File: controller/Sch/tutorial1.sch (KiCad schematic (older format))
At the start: 4 parts

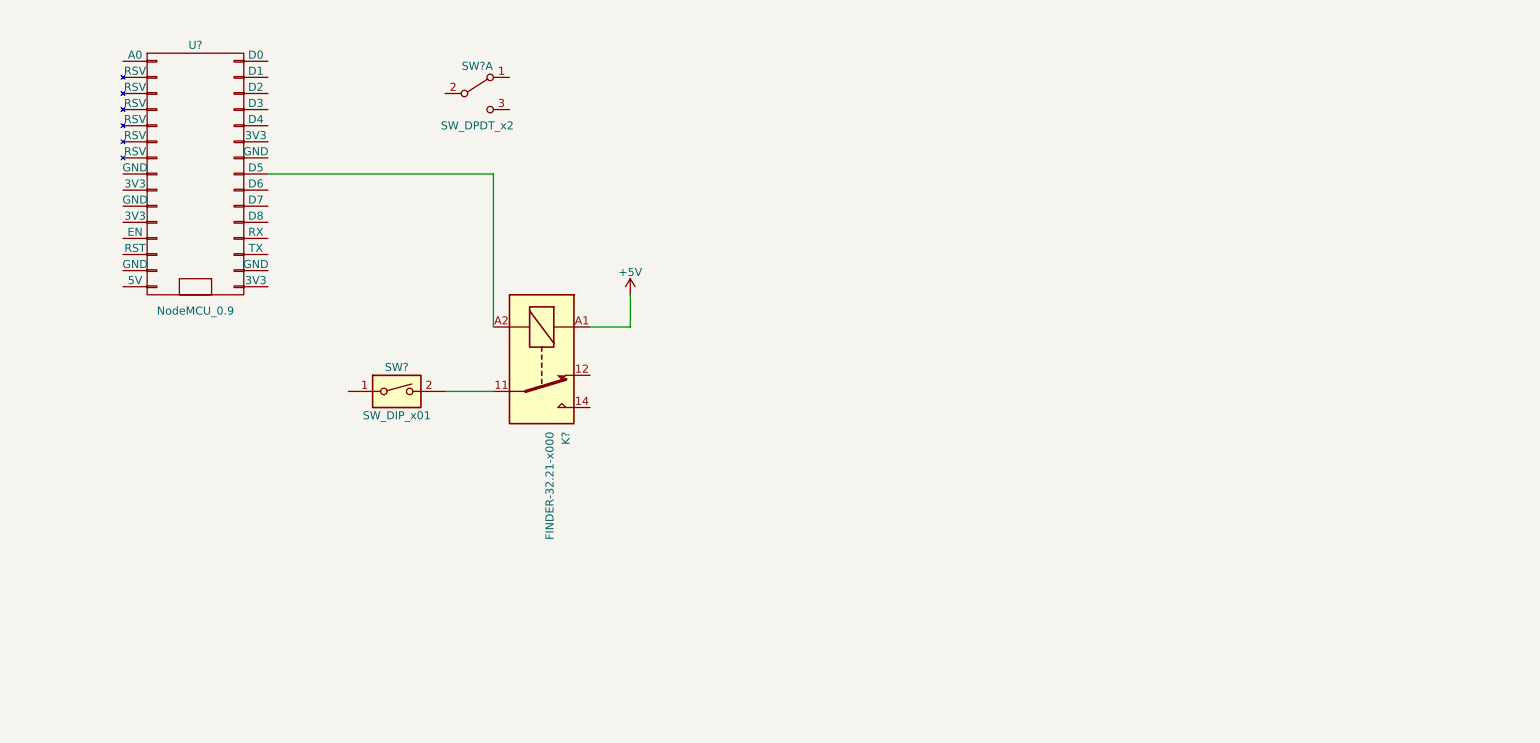
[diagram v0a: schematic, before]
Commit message: Added couple of the switches circuits.
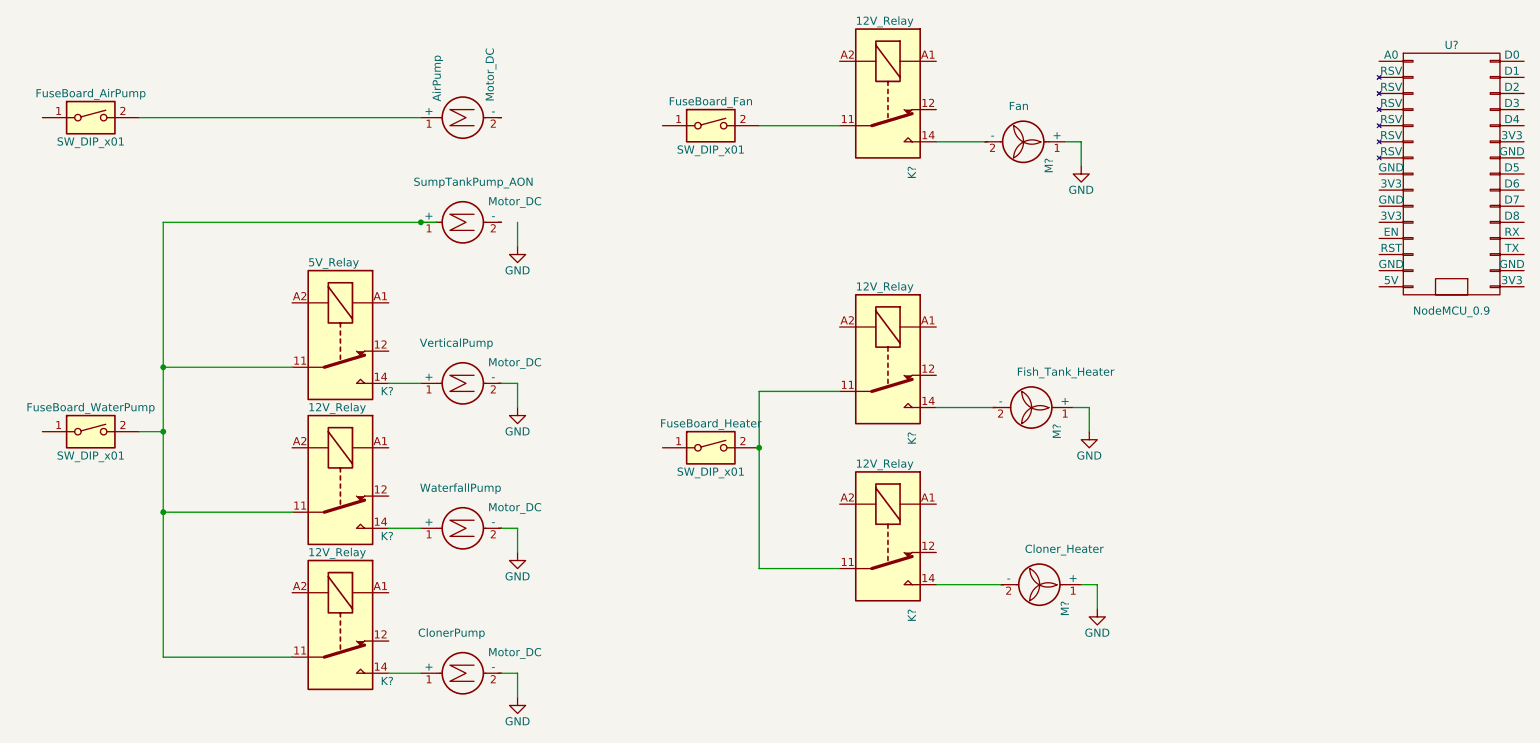
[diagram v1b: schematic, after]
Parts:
- removed SW?: SW_DPDT_x2, symbol SW_DPDT_x2
- added AirPump, ClonerPump, SumpTankPump_AON, VerticalPump, WaterfallPump: Motor_DC, symbol Motor_DC
- added FuseBoard_Fan, FuseBoard_Heater, FuseBoard_WaterPump: SW_DIP_x01, symbol SW_DIP_x01
- added K? (x5): 12V_Relay, Relays_THT:Relay_SPST_Finder_32.21-x300, symbol FINDER-32.21-x000
- added M?: Fan, symbol Fan
- added M?: Fish_Tank_Heater, symbol Fan
- added M?: Cloner_Heater, symbol Fan
- K?: value FINDER-32.21-x000 -> 5V_Relay
- gave numbers to parts that had none: 1
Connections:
- net labels added: GND
- net labels removed: +5V
- wire segments 5 -> 30
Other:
- moved on the sheet: FuseBoard_AirPump, K?, U?
